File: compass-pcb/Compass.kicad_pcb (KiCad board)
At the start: 2 copper layers, 14 parts

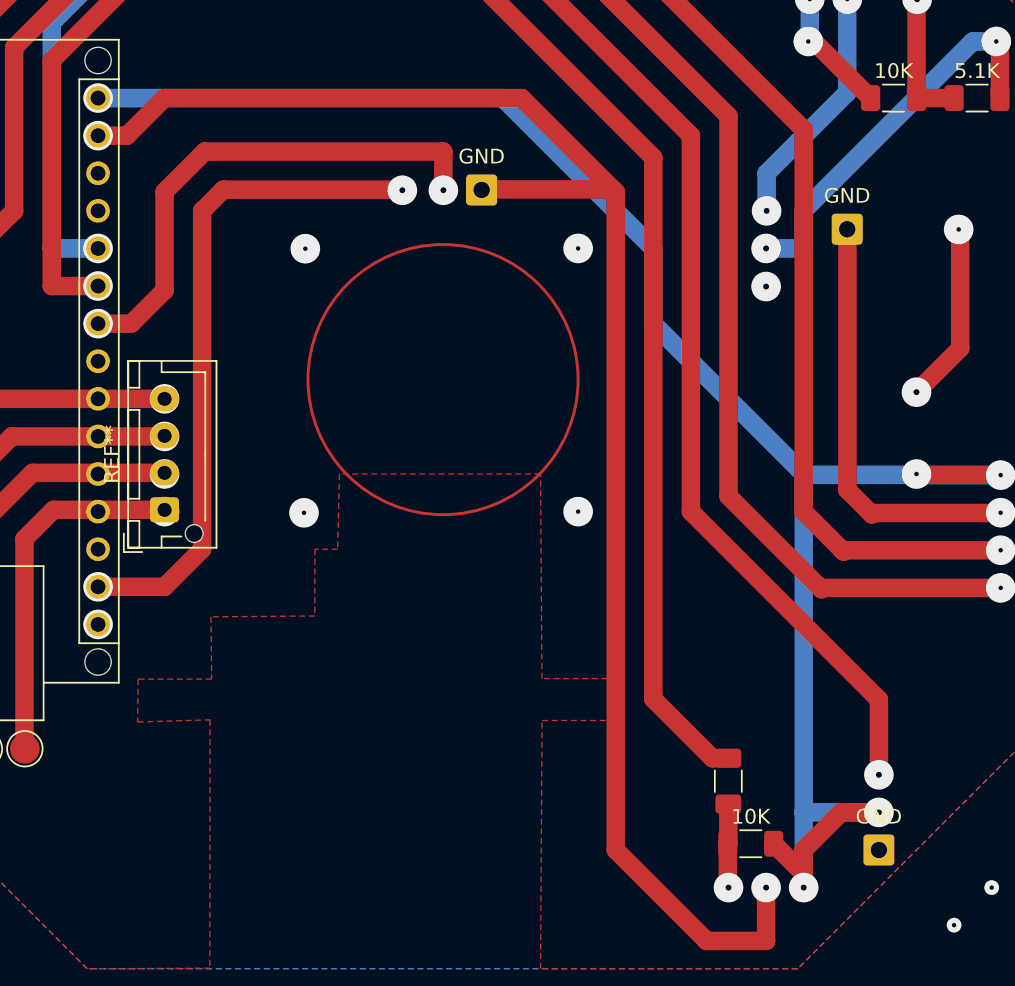
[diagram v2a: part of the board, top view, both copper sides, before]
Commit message: Update Compass.kicad_pcb
fixed error in hall sensor position
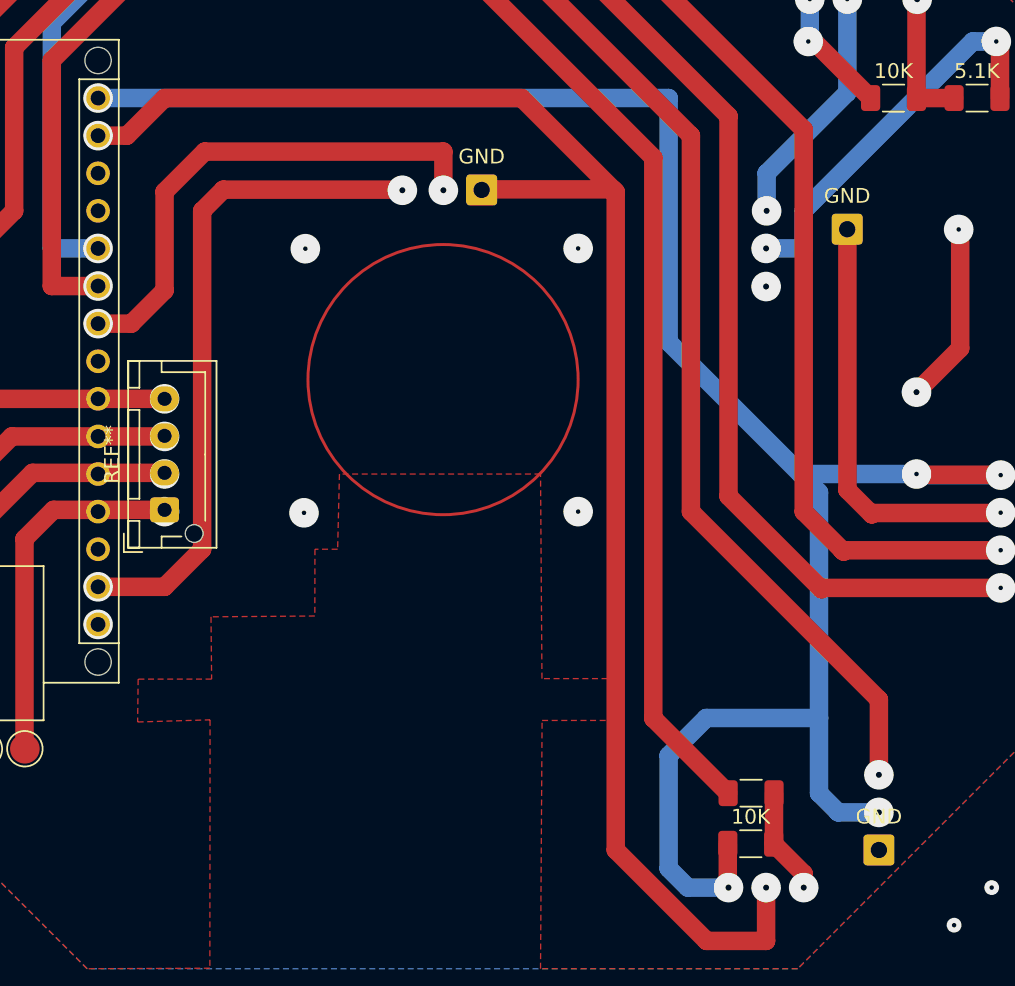
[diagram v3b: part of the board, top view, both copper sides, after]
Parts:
- moved 5.1K 1.74 mm to (168.1, 121.9), turned to 0 degrees
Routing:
- net (no net): track 962.6 -> 980.3 mm
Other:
- board text added: "Always check correct position for the hall sensor!"

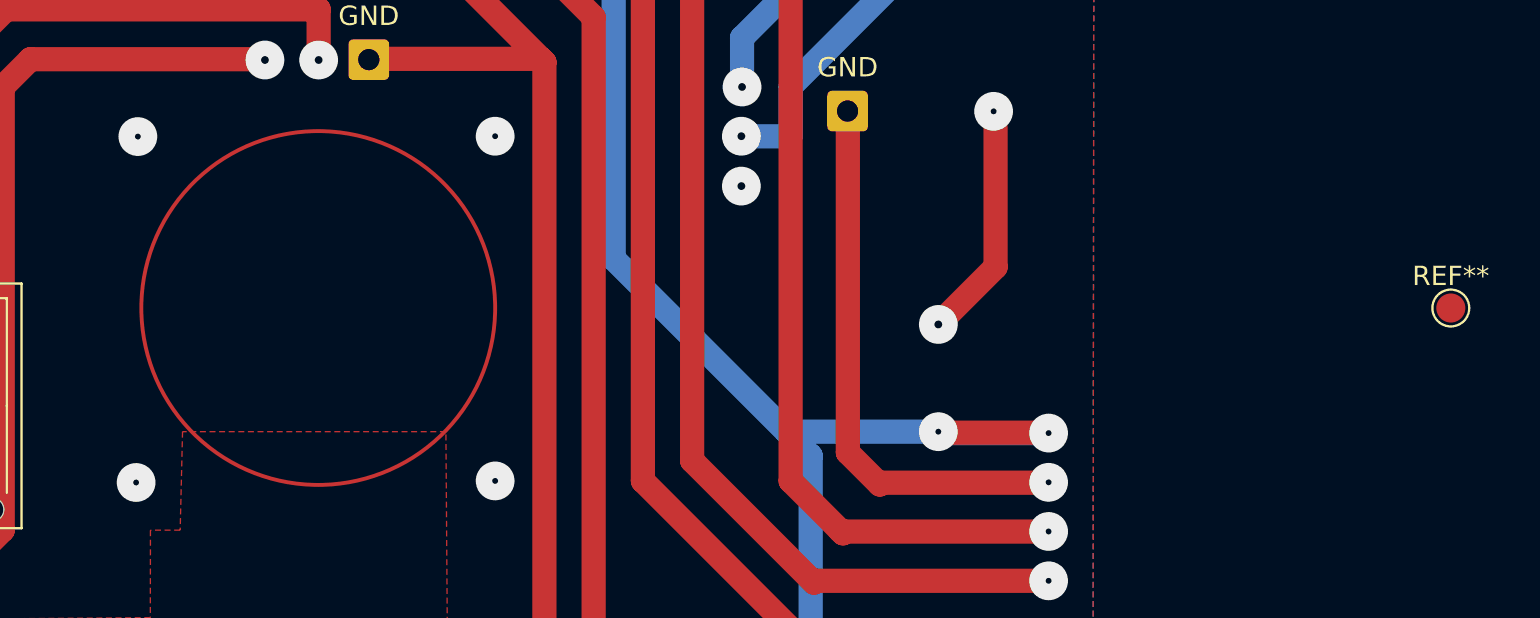
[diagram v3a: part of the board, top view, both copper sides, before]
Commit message: fixing mount holes
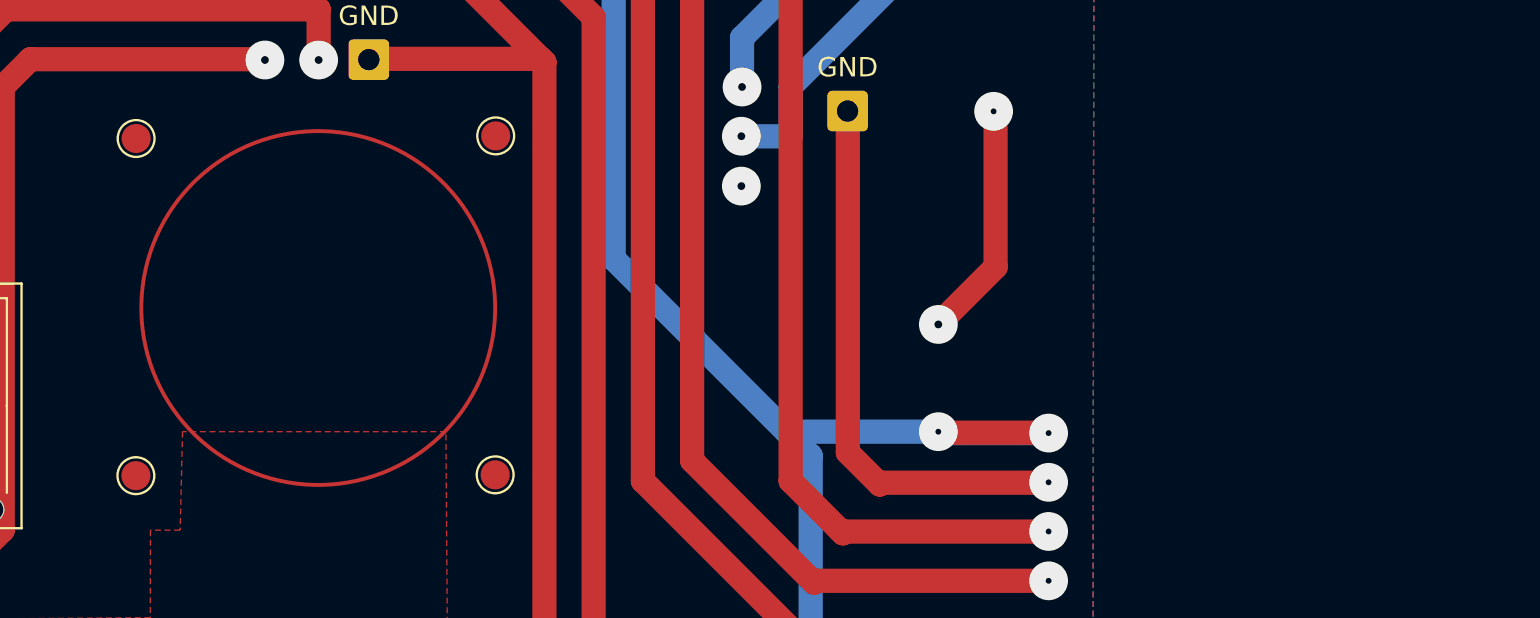
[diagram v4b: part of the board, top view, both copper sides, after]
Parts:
- removed the REF** at (205.7, 94.0)
- added REF**: , TestPoint:TestPoint_Pad_D1.5mm, F.Cu at (156.4, 102.6)
- added REF**: , TestPoint:TestPoint_Pad_D1.5mm, F.Cu at (137.9, 85.2)
- added REF**: , TestPoint:TestPoint_Pad_D1.5mm, F.Cu at (137.9, 102.6)
- added REF**: , TestPoint:TestPoint_Pad_D1.5mm, F.Cu at (156.5, 85.1)
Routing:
- net (no net): vias 51 -> 47
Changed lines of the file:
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@@
     )
+  )
+  (footprint "TestPoint:TestPoint_Pad_D1.5mm" (layer "F.Cu")
+    (at 156.44605 102.585438)
+    (descr "SMD pad as test Point, diameter 1.5mm")
+    (tags "test point SMD pad")
+    (attr exclude_from_pos_files exclude_from_bom)
+    (fp_text reference "REF**" (at -2.54 -5.078) (layer "F.SilkS") hide
+        (effects (font (size 1 1) (thickness 0.15)))
+    )
+    (fp_text value " " (at 0 1.75) (layer "F.Fab")
+        (effects (font (size 1 1) (thickness 0.15)))
+    )
+    (fp_circle (center 0 0) (end 0 0.95)
+      (stroke (width 0.12) (type solid)) (fill none) (layer "F.SilkS"))
+    (fp_circle (center 0 0) (end 1.25 0)
+      (stroke (width 0.05) (type solid)) (fill none) (layer "F.CrtYd"))
+    (pad " " smd circle (at 0 0) (size 1.5 1.5) (layers "F.Cu" "F.Mask"))
+  )
+  (footprint "TestPoint:TestPoint_Pad_D1.5mm" (layer "F.Cu")
+    (at 137.926134 85.2369)
+    (descr "SMD pad as test Point, diameter 1.5mm")
+    (tags "test point SMD pad")
+    (attr exclude_from_pos_files exclude_from_bom)
+    (fp_text reference "REF**" (at 0 -1.648) (layer "F.SilkS") hide
+        (effects (font (size 1 1) (thickness 0.15)))
+    )
+    (fp_text value " " (at 0 1.75) (layer "F.Fab") hide
+        (effects (font (size 1 1) (thickness 0.15)))
+    )
+    (fp_circle (center 0 0) (end 0 0.95)
+      (stroke (width 0.12) (type solid)) (fill none) (layer "F.SilkS"))
+    (fp_circle (center 0 0) (end 1.25 0)
+      (stroke (width 0.05) (type solid)) (fill none) (layer "F.CrtYd"))
+    (pad " " smd circle (at 0 0) (size 1.5 1.5) (layers "F.Cu" "F.Mask"))
   )
   (footprint "Resistor_SMD:R_1206_3216Metric_Pad1.30x1.75mm_HandSolder" (layer "F.Cu")
@@
     )
   )
-  (footprint "TestPoint:TestPoint_Pad_D1.5mm" (layer "F.Cu")
-    (at 205.74 93.98)
-    (descr "SMD pad as test Point, diameter 1.5mm")
-    (tags "test point SMD pad")
-    (attr exclude_from_pos_files exclude_from_bom)
-    (fp_text reference "REF**" (at 0 -1.648) (layer "F.SilkS")
-        (effects (font (size 1 1) (thickness 0.15)))
-    )
-    (fp_text value "TestPoint_Pad_D1.5mm" (at 0 1.75) (layer "F.Fab")
-        (effects (font (size 1 1) (thickness 0.15)))
-    )
-    (fp_text user "${REFERENCE}" (at 0 -1.65) (layer "F.Fab")
-        (effects (font (size 1 1) (thickness 0.15)))
-    )
-    (fp_circle (center 0 0) (end 0 0.95)
-      (stroke (width 0.12) (type solid)) (fill none) (layer "F.SilkS"))
-    (fp_circle (center 0 0) (end 1.25 0)
-      (stroke (width 0.05) (type solid)) (fill none) (layer "F.CrtYd"))
-    (pad "1" smd circle (at 0 0) (size 1.5 1.5) (layers "F.Cu" "F.Mask"))
-  )
   (footprint "TestPoint:TestPoint_Pad_D2.0mm" (layer "F.Cu")
     (at 111.106514 118.967119)
@@
       (rotate (xyz 0 0 0))
     )
+  )
+  (footprint "TestPoint:TestPoint_Pad_D1.5mm" (layer "F.Cu")
+    (at 137.914671 102.627364)
+    (descr "SMD pad as test Point, diameter 1.5mm")
+    (tags "test point SMD pad")
+    (attr exclude_from_pos_files exclude_from_bom)
+    (fp_text reference "REF**" (at -2.54 -5.078) (layer "F.SilkS") hide
+        (effects (font (size 1 1) (thickness 0.15)))
+    )
+    (fp_text value " " (at 0 1.75) (layer "F.Fab")
+        (effects (font (size 1 1) (thickness 0.15)))
+    )
+    (fp_circle (center 0 0) (end 0 0.95)
+      (stroke (width 0.12) (type solid)) (fill none) (layer "F.SilkS"))
+    (fp_circle (center 0 0) (end 1.25 0)
+      (stroke (width 0.05) (type solid)) (fill none) (layer "F.CrtYd"))
+    (pad " " smd circle (at 0 0) (size 1.5 1.5) (layers "F.Cu" "F.Mask"))
+  )
+  (footprint "TestPoint:TestPoint_Pad_D1.5mm" (layer "F.Cu")
+    (at 156.473771 85.102214)
+    (descr "SMD pad as test Point, diameter 1.5mm")
+    (tags "test point SMD pad")
+    (attr exclude_from_pos_files exclude_from_bom)
+    (fp_text reference "REF**" (at 2.54 -2.54) (layer "F.SilkS") hide
+        (effects (font (size 1 1) (thickness 0.15)))
+    )
+    (fp_text value " " (at 0 1.75) (layer "F.Fab")
+        (effects (font (size 1 1) (thickness 0.15)))
+    )
+    (fp_circle (center 0 0) (end 0 0.95)
+      (stroke (width 0.12) (type solid)) (fill none) (layer "F.SilkS"))
+    (fp_circle (center 0 0) (end 1.25 0)
+      (stroke (width 0.05) (type solid)) (fill none) (layer "F.CrtYd"))
+    (pad " " smd circle (at 0 0) (size 1.5 1.5) (layers "F.Cu" "F.Mask"))
   )
   (footprint "Module:Arduino_Nano_WithMountingHoles" (layer "F.Cu")
@@
   (via (at 108.699687 85.096606) (size 2) (drill 0.4) (layers "F.Cu" "B.Cu") (net 0))
   (via (at 110.725445 125.758533) (size 1) (drill 0.3) (layers "F.Cu" "B.Cu") (net 0))
-  (via (at 138.015892 85.135753) (size 2) (drill 0.3) (layers "F.Cu" "B.Cu") (net 0))
   (via (at 124.013168 85.118533) (size 2) (drill 0.4) (layers "F.Cu" "B.Cu") (net 0))
   (via (at 166.605445 128.298533) (size 2) (drill 0.4) (layers "F.Cu" "B.Cu") (net 0))
@@
   (via (at 176.765445 123.218533) (size 2) (drill 0.4) (layers "F.Cu" "B.Cu") (net 0))
   (via (at 147.341357 81.187222) (size 2) (drill 0.4) (layers "F.Cu" "B.Cu") (net 0))
-  (via (at 137.925772 102.979598) (size 2) (drill 0.3) (layers "F.Cu" "B.Cu") (net 0))
   (via (at 181.845445 59.718533) (size 1) (drill 0.3) (layers "F.Cu" "B.Cu") (net 0))
   (via (at 176.765445 120.678533) (size 2) (drill 0.4) (layers "F.Cu" "B.Cu") (net 0))
@@
   (via (at 184.993201 100.431017) (size 2) (drill 0.3) (layers "F.Cu" "B.Cu") (net 0))
   (via (at 184.696358 71.135847) (size 2) (drill 0.3) (layers "F.Cu" "B.Cu") (net 0))
-  (via (at 156.445445 102.898533) (size 2) (drill 0.3) (layers "F.Cu" "B.Cu") (net 0))
   (via (at 128.505445 102.898533) (size 2) (drill 0.3) (layers "F.Cu" "B.Cu") (net 0))
   (via (at 186.925445 54.638533) (size 1) (drill 0.3) (layers "F.Cu" "B.Cu") (net 0))
@@
   (via (at 108.185445 54.638533) (size 1) (drill 0.3) (layers "F.Cu" "B.Cu") (net 0))
   (via (at 184.993201 108.051017) (size 2) (drill 0.3) (layers "F.Cu" "B.Cu") (net 0))
-  (via (at 156.445445 85.118533) (size 2) (drill 0.3) (layers "F.Cu" "B.Cu") (net 0))
   (via (at 128.505445 95.278533) (size 2) (drill 0.3) (layers "F.Cu" "B.Cu") (net 0))
   (via (at 171.996358 71.135847) (size 2) (drill 0.3) (layers "F.Cu" "B.Cu") (net 0))
@@
     (connect_pads (clearance 1.25))
     (min_thickness 0.5) (filled_areas_thickness no)
-    (fill yes (thermal_gap 1) (thermal_bridge_width 1) (island_removal_mode 1) (island_area_min 10))
+    (fill (thermal_gap 1) (thermal_bridge_width 1) (island_removal_mode 1) (island_area_min 10))
     (polygon
       (pts
@@
     (connect_pads (clearance 1.25))
     (min_thickness 0.5) (filled_areas_thickness no)
-    (fill yes (thermal_gap 1) (thermal_bridge_width 1) (island_removal_mode 1) (island_area_min 10))
+    (fill (thermal_gap 1) (thermal_bridge_width 1) (island_removal_mode 1) (island_area_min 10))
     (polygon
       (pts
